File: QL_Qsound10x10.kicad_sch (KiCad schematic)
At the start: 23 parts, among them J1 QL_SLOT_DIN41612_CARD, J2 Conn_02x17_Odd_Even, J3 AudioJack2_Ground_Switch, J4 Conn_01x01_Female, Q1 PN2222A, U1 L7805, U2 74LS10, U3 74LS266, U4 W27C512, U5 74LS03, U6 PSG_AY-3-8910, U7 6821

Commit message: update info
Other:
- title: Kempston Interface Disc for Sinclair QL -> QSound/Qprint Interface for Sinclair QL
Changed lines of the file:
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@@
   (paper "A3")
   (title_block
-    (title "Kempston Interface Disc for Sinclair QL")
-    (date "2021-09-12")
+    (title "QSound/Qprint Interface for Sinclair QL")
+    (date "2022-09-26")
     (rev "0.0a")
     (company "Alvaro Alea Fdz")

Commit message: complete strings in pcb
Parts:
- R1: value 100k -> 2k2
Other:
- note added: "* Original R1 value 1K"
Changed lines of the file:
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@@
     (stroke (width 0) (type default) (color 0 0 0 0))
   )
+  (text "* Original R1 value 1K" (at 84.836 125.349 0)
+    (effects (font (size 1.27 1.27)) (justify left bottom))
+  )
   (label "D6" (at 28.448 42.291 0)
     (effects (font (size 1.27 1.27)) (justify left bottom))
@@
     (effects (font (size 1.27 1.27)) (justify left bottom))
   )
-  (label "A15" (at 58.928 57.531 0)
+  (label "A15" (at 62.992 57.531 0)
     (effects (font (size 1.27 1.27)) (justify left bottom))
   )
@@
     (effects (font (size 1.27 1.27)) (justify left bottom))
   )
-  (label "A1" (at 58.928 90.551 0)
+  (label "A1" (at 64.135 90.551 0)
     (effects (font (size 1.27 1.27)) (justify left bottom))
   )
@@
     (effects (font (size 1.27 1.27)) (justify left bottom))
   )
-  (label "A0" (at 58.928 85.471 0)
+  (label "A0" (at 64.262 85.471 0)
     (effects (font (size 1.27 1.27)) (justify left bottom))
   )
@@
     (effects (font (size 1.27 1.27)) (justify left bottom))
   )
-  (label "A2" (at 58.928 93.091 0)
+  (label "A2" (at 64.008 93.091 0)
     (effects (font (size 1.27 1.27)) (justify left bottom))
   )
@@
   (symbol (lib_id "Device:R") (at 81.026 128.651 0) (unit 1)
     (in_bom yes) (on_board yes) (fields_autoplaced)
-    (property "Reference" "R1" (id 0) (at 82.931 127.3809 0)
-      (effects (font (size 1.27 1.27)) (justify left))
-    )
-    (property "Value" "100k" (id 1) (at 82.931 129.9209 0)
+    (property "Reference" "R1" (id 0) (at 83.82 127.3809 0)
+      (effects (font (size 1.27 1.27)) (justify left))
+    )
+    (property "Value" "2k2" (id 1) (at 83.82 129.9209 0)
       (effects (font (size 1.27 1.27)) (justify left))
     )
@@
     )
     (path "/f84563fa-8835-4ca8-a201-d0310a3b7d1b"
-      (reference "R1") (unit 1) (value "100k") (footprint "Resistor_THT:R_Axial_DIN0207_L6.3mm_D2.5mm_P7.62mm_Horizontal")
+      (reference "R1") (unit 1) (value "2k2") (footprint "Resistor_THT:R_Axial_DIN0207_L6.3mm_D2.5mm_P7.62mm_Horizontal")
     )
     (path "/f3b434c3-f33c-4418-9114-1429ce9d457f"

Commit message: Update, now work all
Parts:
- Q1: value PN2222A -> 2N2222A
- U6: value PSG_AY-3-8910 -> AY-3-8910
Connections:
- net DS: now also U5.2
- net E: now also U5.12, U5.13; no longer U5.2
- net at Q1.2 (B), U2.8, U5.5: no longer U5.4
- net at U5.11: now also U5.4
- net DTACK: now reaches J1.b25 (~{DTACK})
- no-connect marks 54 -> 50
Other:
- moved on the sheet: C2, C3, C4, C5, J1, J2, J3, J4, Q1, R1, R2, R3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

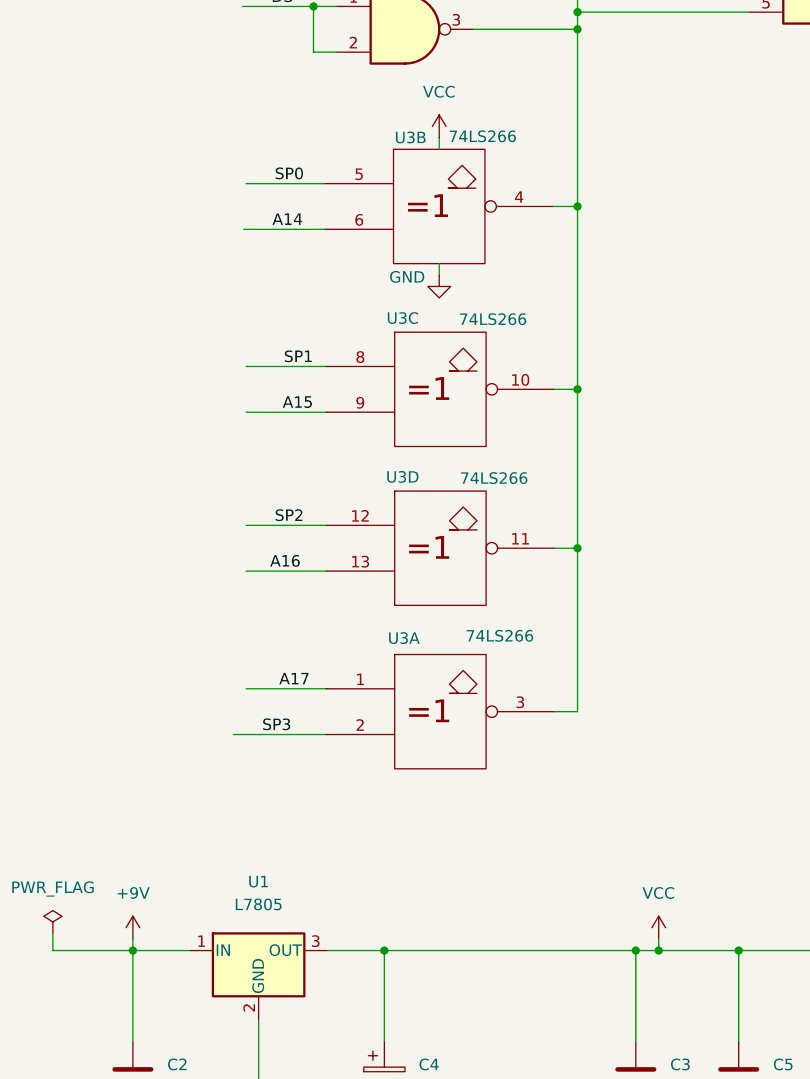
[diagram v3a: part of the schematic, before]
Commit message: tracks more similar to original
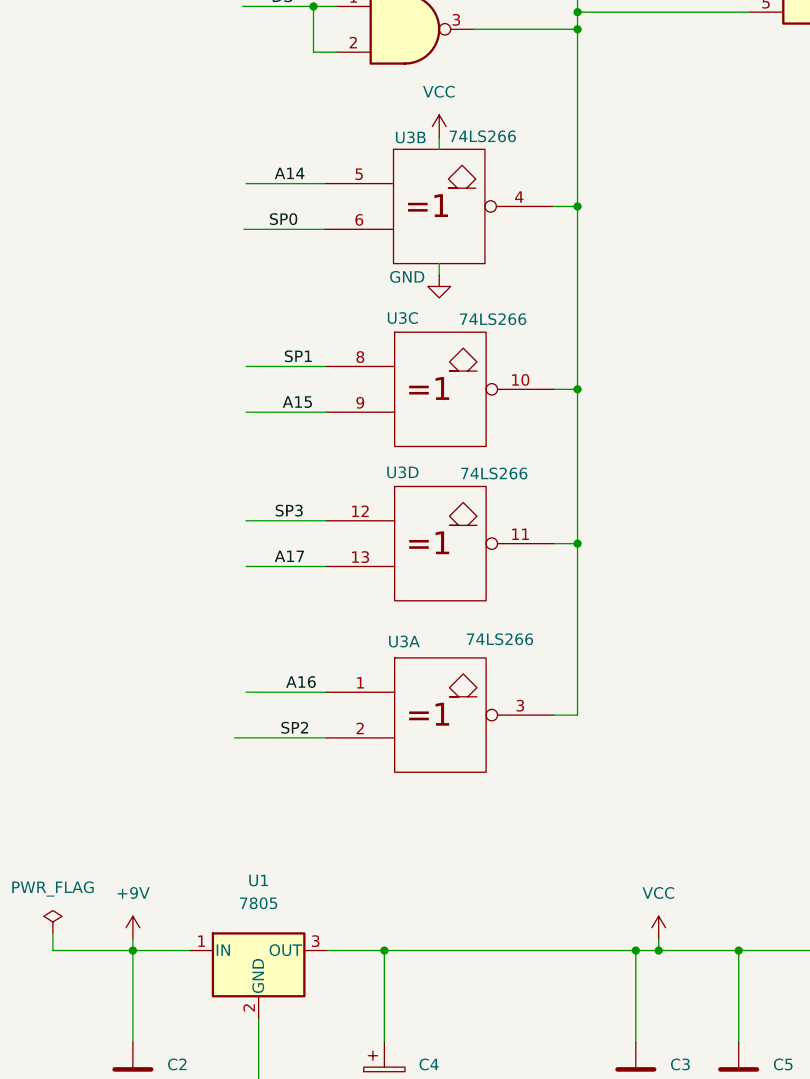
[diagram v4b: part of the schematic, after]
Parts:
- U1: value L7805 -> 7805
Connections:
- net A14: now also U3.5; no longer U3.6
- net A16: now also U3.1; no longer U3.13
- net A17: now also U3.13; no longer U3.1
- net SP0: now also U3.6; no longer U3.5
- net SP2: now also U3.2; no longer U3.12
- net SP3: now also U3.12; no longer U3.2
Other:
- moved on the sheet: U3D
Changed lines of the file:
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@@
   (junction (at 102.362 251.587) (diameter 0) (color 0 0 0 0)
   )
+  (junction (at 84.455 206.375) (diameter 0) (color 0 0 0 0)
+  )
   (junction (at 144.018 144.78) (diameter 0) (color 0 0 0 0)
   )
@@
   )
   (junction (at 273.685 100.965) (diameter 0) (color 0 0 0 0)
-  )
-  (junction (at 84.455 206.883) (diameter 0) (color 0 0 0 0)
   )
   (junction (at 77.47 17.145) (diameter 0) (color 0 0 0 0)
@@
     (stroke (width 0) (type default) (color 0 0 0 0))
   )
-  (wire (pts (xy 46.228 227.584) (xy 56.515 227.584))
+  (wire (pts (xy 46.355 227.965) (xy 56.515 227.965))
     (stroke (width 0) (type default) (color 0 0 0 0))
   )
@@
     (stroke (width 0) (type default) (color 0 0 0 0))
   )
-  (wire (pts (xy 84.455 225.044) (xy 81.915 225.044))
+  (wire (pts (xy 84.455 225.425) (xy 81.915 225.425))
     (stroke (width 0) (type default) (color 0 0 0 0))
   )
@@
     (stroke (width 0) (type default) (color 0 0 0 0))
   )
-  (wire (pts (xy 47.625 204.343) (xy 56.515 204.343))
+  (wire (pts (xy 47.625 203.835) (xy 56.515 203.835))
     (stroke (width 0) (type default) (color 0 0 0 0))
   )
@@
     (stroke (width 0) (type default) (color 0 0 0 0))
   )
-  (wire (pts (xy 84.455 189.23) (xy 84.455 206.883))
-    (stroke (width 0) (type default) (color 0 0 0 0))
-  )
-  (wire (pts (xy 84.455 206.883) (xy 84.455 225.044))
+  (wire (pts (xy 84.455 189.23) (xy 84.455 206.375))
+    (stroke (width 0) (type default) (color 0 0 0 0))
+  )
+  (wire (pts (xy 84.455 206.375) (xy 84.455 225.425))
     (stroke (width 0) (type default) (color 0 0 0 0))
   )
@@
     (stroke (width 0) (type default) (color 0 0 0 0))
   )
-  (wire (pts (xy 47.625 222.504) (xy 56.515 222.504))
+  (wire (pts (xy 47.625 222.885) (xy 56.515 222.885))
     (stroke (width 0) (type default) (color 0 0 0 0))
   )
@@
     (stroke (width 0) (type default) (color 0 0 0 0))
   )
-  (wire (pts (xy 81.915 206.883) (xy 84.455 206.883))
+  (wire (pts (xy 81.915 206.375) (xy 84.455 206.375))
     (stroke (width 0) (type default) (color 0 0 0 0))
   )
@@
     (stroke (width 0) (type default) (color 0 0 0 0))
   )
-  (wire (pts (xy 47.625 209.423) (xy 56.515 209.423))
+  (wire (pts (xy 47.625 208.915) (xy 56.515 208.915))
     (stroke (width 0) (type default) (color 0 0 0 0))
   )
@@
     (effects (font (size 1.27 1.27)) (justify left bottom))
   )
-  (label "SP2" (at 50.8 204.343 0)
+  (label "SP2" (at 51.435 227.965 0)
     (effects (font (size 1.27 1.27)) (justify left bottom))
   )
@@
     (effects (font (size 1.27 1.27)) (justify left bottom))
   )
-  (label "A17" (at 51.308 222.504 0)
+  (label "A17" (at 50.8 208.915 0)
     (effects (font (size 1.27 1.27)) (justify left bottom))
   )
@@
     (effects (font (size 1.27 1.27)) (justify left bottom))
   )
-  (label "SP0" (at 50.8 166.37 0)
+  (label "SP0" (at 50.165 171.45 0)
     (effects (font (size 1.27 1.27)) (justify left bottom))
   )
@@
     (effects (font (size 1.27 1.27)) (justify left bottom))
   )
-  (label "A14" (at 50.546 171.45 0)
+  (label "A14" (at 50.8 166.37 0)
     (effects (font (size 1.27 1.27)) (justify left bottom))
   )
@@
     (effects (font (size 1.27 1.27)) (justify left bottom))
   )
-  (label "SP3" (at 49.403 227.584 0)
+  (label "SP3" (at 50.8 203.835 0)
     (effects (font (size 1.27 1.27)) (justify left bottom))
   )
@@
     (effects (font (size 1.27 1.27)) (justify left bottom))
   )
-  (label "A16" (at 50.292 209.423 0)
+  (label "A16" (at 52.07 222.885 0)
     (effects (font (size 1.27 1.27)) (justify left bottom))
   )
@@
     (pin "1")
   )
-  (symbol (lib_id "74xx_IEEE:74LS266") (at 69.215 206.883 0) (unit 4)
+  (symbol (lib_id "74xx_IEEE:74LS266") (at 69.215 206.375 0) (unit 4)
     (in_bom yes) (on_board yes)
-    (property "Reference" "U3" (id 0) (at 65.024 199.009 0))
-    (property "Value" "74LS266" (id 1) (at 75.184 199.136 0))
-    (property "Footprint" "Package_DIP:DIP-14_W7.62mm_LongPads" (id 2) (at 69.215 206.883 0)
-      (effects (font (size 1.27 1.27)) hide)
-    )
-    (property "Datasheet" "" (id 3) (at 69.215 206.883 0)
+    (property "Reference" "U3" (id 0) (at 65.024 198.501 0))
+    (property "Value" "74LS266" (id 1) (at 75.184 198.628 0))
+    (property "Footprint" "Package_DIP:DIP-14_W7.62mm_LongPads" (id 2) (at 69.215 206.375 0)
+      (effects (font (size 1.27 1.27)) hide)
+    )
+    (property "Datasheet" "" (id 3) (at 69.215 206.375 0)
       (effects (font (size 1.27 1.27)) hide)
     )
@@
     (pin "1")
   )
-  (symbol (lib_id "74xx_IEEE:74LS266") (at 69.215 225.044 0) (unit 1)
+  (symbol (lib_id "74xx_IEEE:74LS266") (at 69.215 225.425 0) (unit 1)
     (in_bom yes) (on_board yes)
-    (property "Reference" "U3" (id 0) (at 65.151 216.916 0))
-    (property "Value" "74LS266" (id 1) (at 75.819 216.662 0))
-    (property "Footprint" "Package_DIP:DIP-14_W7.62mm_LongPads" (id 2) (at 69.215 225.044 0)
-      (effects (font (size 1.27 1.27)) hide)
-    )
-    (property "Datasheet" "" (id 3) (at 69.215 225.044 0)
+    (property "Reference" "U3" (id 0) (at 65.151 217.297 0))
+    (property "Value" "74LS266" (id 1) (at 75.819 217.043 0))
+    (property "Footprint" "Package_DIP:DIP-14_W7.62mm_LongPads" (id 2) (at 69.215 225.425 0)
+      (effects (font (size 1.27 1.27)) hide)
+    )
+    (property "Datasheet" "" (id 3) (at 69.215 225.425 0)
       (effects (font (size 1.27 1.27)) hide)
     )
@@
   (symbol (lib_id "Regulator_Linear:L7805") (at 49.022 251.587 0) (unit 1)
     (in_bom yes) (on_board yes) (fields_autoplaced)
-    (property "Reference" "U1" (id 0) (at 49.022 243.967 0))
-    (property "Value" "L7805" (id 1) (at 49.022 246.507 0))
+    (property "Reference" "U1" (id 0) (at 49.022 243.84 0))
+    (property "Value" "7805" (id 1) (at 49.022 246.38 0))
     (property "Footprint" "Package_TO_SOT_THT:TO-220-3_Horizontal_TabDown" (id 2) (at 49.657 255.397 0)
       (effects (font (size 1.27 1.27) italic) (justify left) hide)
@@
     )
     (path "/7ed51b93-9249-431f-80b5-6736ef3b2086"
-      (reference "U1") (unit 1) (value "L7805") (footprint "Package_TO_SOT_THT:TO-220-3_Horizontal_TabDown")
+      (reference "U1") (unit 1) (value "7805") (footprint "Package_TO_SOT_THT:TO-220-3_Horizontal_TabDown")
     )
     (path "/e963a89d-ed13-44e9-bf5c-3ead18fd5d50"

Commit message: Update some errors in PCB
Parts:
- removed J3: AudioJack2_Ground_Switch, 8bits:AudioJack2_Ground_Switch, symbol Connector:AudioJack2_Ground_Switch
- added J3: AudioJack2_Ground_Switch, 8bits:AUDIO-JACK, symbol Connector_Audio:AudioJack2_Ground_Switch
- J4: symbol Connector:Conn_01x01_Female -> Connector:Conn_01x01_Socket; now left out of the parts list
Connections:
- net GND: now also J3.G
- net at R2.2, R7.1: now also J3.S
- net at R7.2: now also J3.T
- net DTACK: no longer names the net of J1.b25 (~{DTACK})
- no-connect marks 50 -> 53
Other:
- note added: "N/C"
- note added: "PGM"
- note added: "Vpp"
- moved on the sheet: U2A, U3A, U3B, U3C, U3D, U5C

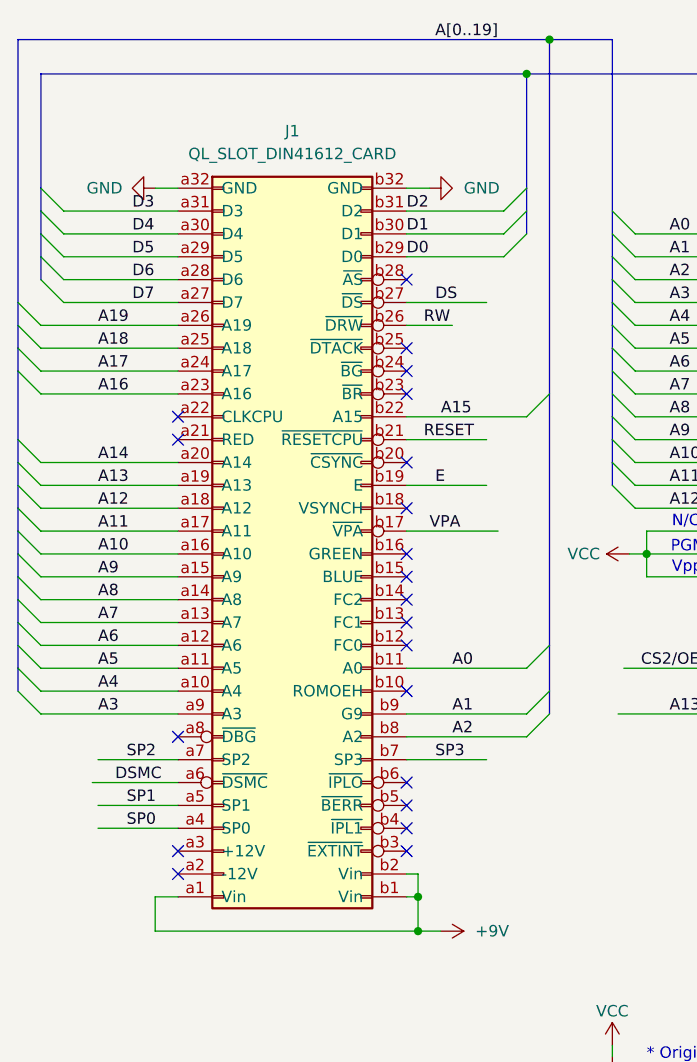
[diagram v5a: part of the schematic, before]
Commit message: Updated pins on QL conector
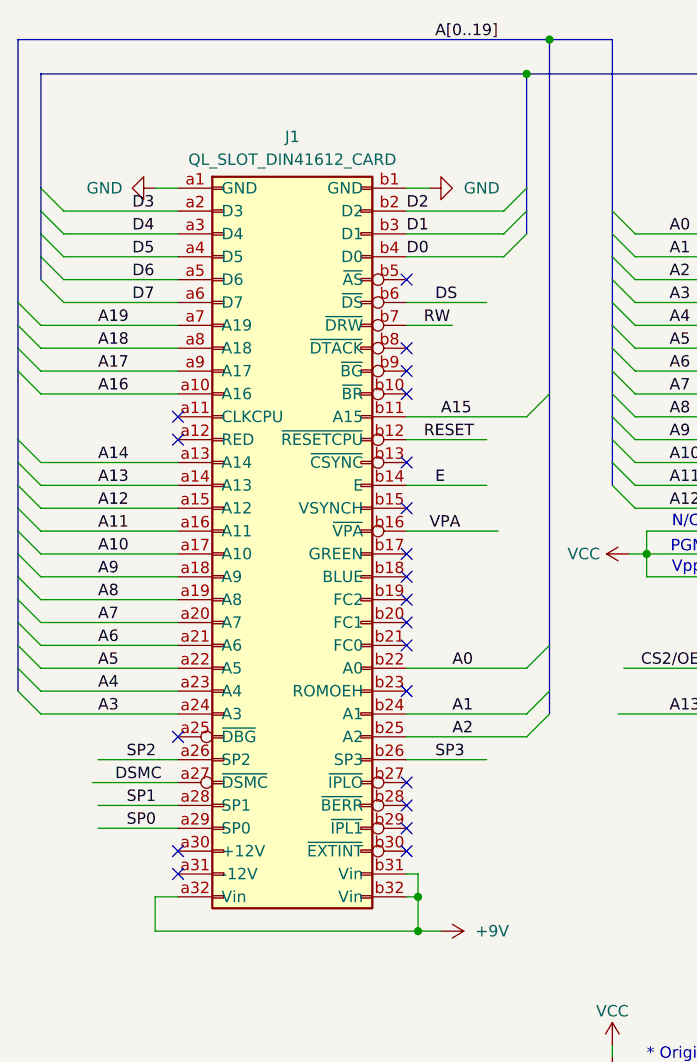
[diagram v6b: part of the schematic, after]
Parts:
- J1: footprint 8bits:DIN41612_B_2x32_Male_Horizontal_THT -> 8bits:DIN41612_B_2x32_Female_Horizontal_THT; symbol 8bits:QL_SLOT_DIN41612_CARD -> 8bits:QL_SLOT_DIN41612
- J3: footprint 8bits:AUDIO-JACK -> 8bits:AudioJack2_Ground_Switch
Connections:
- net +9V: now also J1.a32 (Vin), J1.b31 (Vin), J1.b32 (Vin); no longer J1.a1 (Vin), J1.b1 (Vin), J1.b2 (Vin)
- net A0: now also J1.b22 (A0); no longer J1.b11 (A0)
- net A1: now also J1.b24 (A1); no longer J1.b9 (G9)
- net A10: now also J1.a17 (A10); no longer J1.a16 (A10)
- net A11: now also J1.a16 (A11); no longer J1.a17 (A11)
- net A12: now also J1.a15 (A12); no longer J1.a18 (A12)
- net A13: now also J1.a14 (A13); no longer J1.a19 (A13)
- net A14: now also J1.a13 (A14); no longer J1.a20 (A14)
- net A15: now also J1.b11 (A15); no longer J1.b22 (A15)
- net A16: now also J1.a10 (A16); no longer J1.a23 (A16)
- net A17: now also J1.a9 (A17); no longer J1.a24 (A17)
- net A18: now also J1.a8 (A18); no longer J1.a25 (A18)
- net A19: now also J1.a7 (A19); no longer J1.a26 (A19)
- net A2: now also J1.b25 (A2); no longer J1.b8 (A2)
- net A3: now also J1.a24 (A3); no longer J1.a9 (A3)
- net A4: now also J1.a23 (A4); no longer J1.a10 (A4)
- net A5: now also J1.a22 (A5); no longer J1.a11 (A5)
- net A6: now also J1.a21 (A6); no longer J1.a12 (A6)
- net A7: now also J1.a20 (A7); no longer J1.a13 (A7)
- net A8: now also J1.a19 (A8); no longer J1.a14 (A8)
- net A9: now also J1.a18 (A9); no longer J1.a15 (A9)
- net D0: now also J1.b4 (D0); no longer J1.b29 (D0)
- net D1: now also J1.b3 (D1); no longer J1.b30 (D1)
- net D2: now also J1.b2 (D2); no longer J1.b31 (D2)
- net D3: now also J1.a2 (D3); no longer J1.a31 (D3)
- net D4: now also J1.a3 (D4); no longer J1.a30 (D4)
- net D5: now also J1.a4 (D5); no longer J1.a29 (D5)
- net D6: now also J1.a5 (D6); no longer J1.a28 (D6)
- net D7: now also J1.a6 (D7); no longer J1.a27 (D7)
- net DS: now also J1.b6 (~{DS}); no longer J1.b27 (~{DS})
- net DSMC: now also J1.a27 (~{DSMC}); no longer J1.a6 (~{DSMC})
- net E: now also J1.b14 (E); no longer J1.b19 (E)
- net GND: now also J1.a1 (GND), J1.b1 (GND); no longer J1.a32 (GND), J1.b32 (GND)
- net RESET: now also J1.b12 (~{RESETCPU}); no longer J1.b21 (~{RESETCPU})
- net RW: now also J1.b7 (~{DRW}); no longer J1.b26 (~{DRW})
- net SP0: now also J1.a29 (SP0); no longer J1.a4 (SP0)
- net SP1: now also J1.a28 (SP1); no longer J1.a5 (SP1)
- net SP2: now also J1.a26 (SP2); no longer J1.a7 (SP2)
- net SP3: now also J1.b26 (SP3); no longer J1.b7 (SP3)
- net VPA: now also J1.b16 (~{VPA}); no longer J1.b17 (~{VPA})
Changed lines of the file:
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@@
   (title_block
     (title "QSound/Qprint Interface for Sinclair QL")
-    (date "2023-11-19")
-    (rev "0.0b")
+    (date "2023-12-26")
+    (rev "0.1b")
     (company "Alvaro Alea Fdz")
   )
@@
       (effects (font (size 1.27 1.27)) (justify right))
     )
-    (property "Footprint" "8bits:AUDIO-JACK" (at 269.24 34.925 0)
+    (property "Footprint" "8bits:AudioJack2_Ground_Switch" (at 269.24 34.925 0)
       (effects (font (size 1.27 1.27)) hide)
     )
@@
     )
   )
-  (symbol (lib_id "8bits:QL_SLOT_DIN41612_CARD") (at 48.895 71.755 0) (unit 1)
+  (symbol (lib_id "8bits:QL_SLOT_DIN41612") (at 48.895 71.755 0) (unit 1)
     (in_bom yes) (on_board yes) (dnp no) (fields_autoplaced)
-    (property "Reference" "J1" (at 48.895 27.305 0)
+    (property "Reference" "J1" (at 48.895 27.94 0)
       (effects (font (size 1.27 1.27)))
     )
-    (property "Value" "QL_SLOT_DIN41612_CARD" (at 48.895 29.845 0)
+    (property "Value" "QL_SLOT_DIN41612_CARD" (at 48.895 30.48 0)
       (effects (font (size 1.27 1.27)))
     )
-    (property "Footprint" "8bits:DIN41612_B_2x32_Male_Horizontal_THT" (at 41.275 71.755 0)
-      (effects (font (size 1.27 1.27)) hide)
-    )
+    (property "Footprint" "8bits:DIN41612_B_2x32_Female_Horizontal_THT" (at 41.275 71.755 0)
+      (effects (font (size 1.27 1.27)) hide)
+    )
